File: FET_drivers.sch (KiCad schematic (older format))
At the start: 41 parts

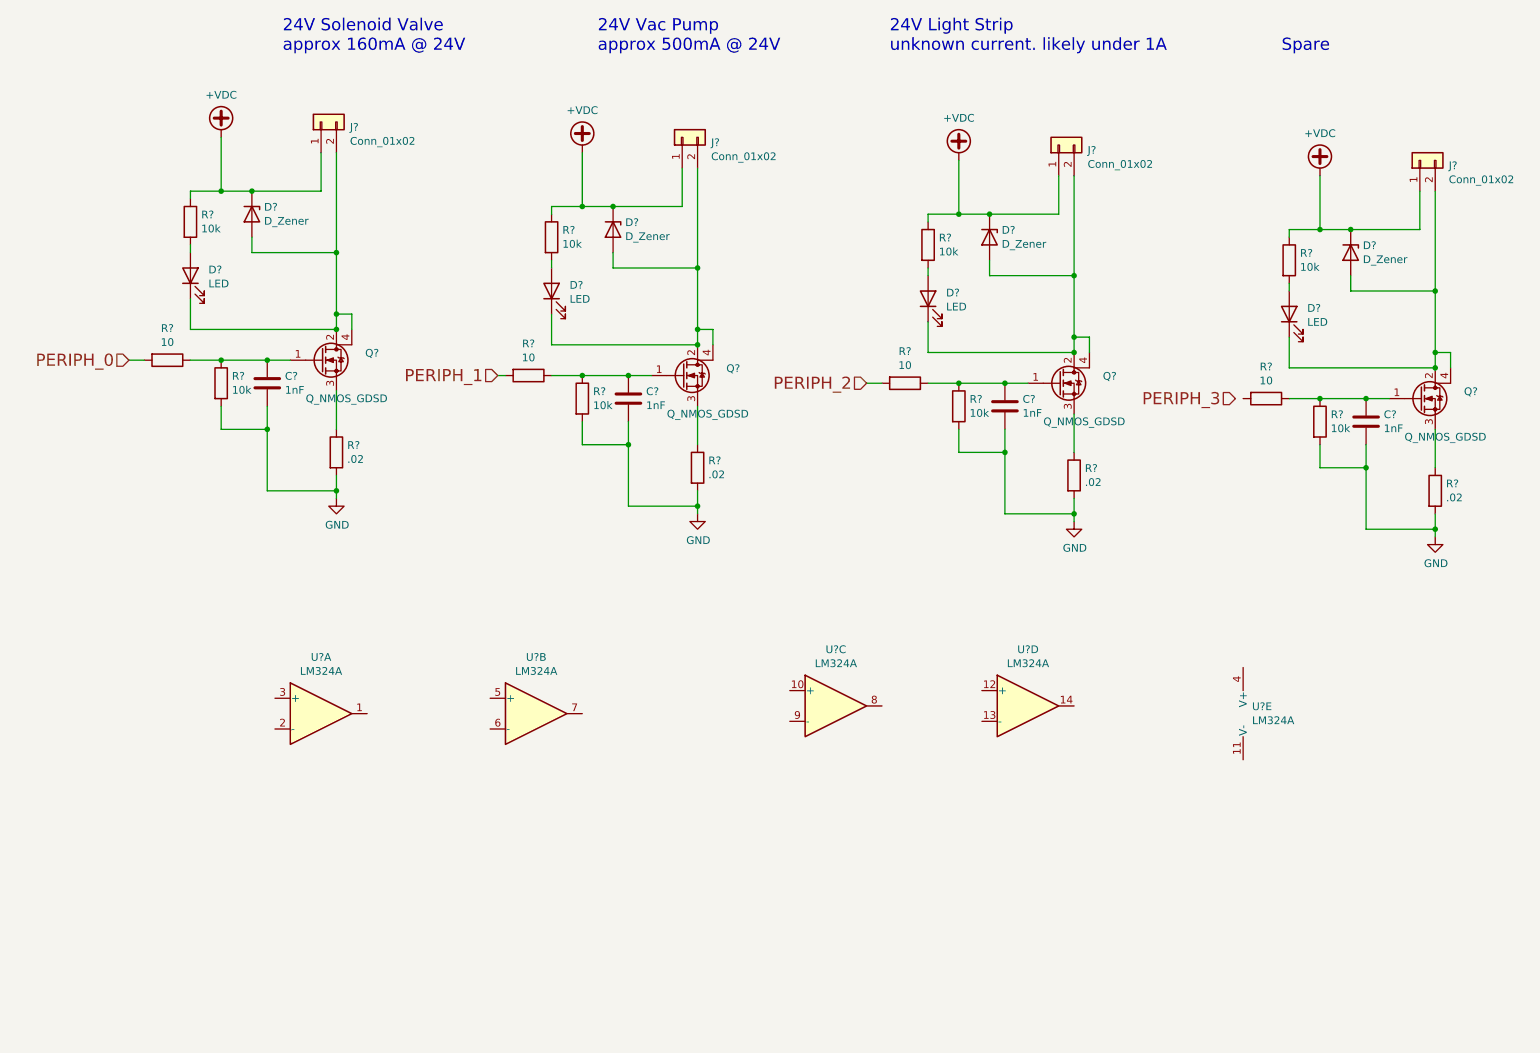
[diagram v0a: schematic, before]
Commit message: Added FET Drivers + PNs. Started Trinamic drivers
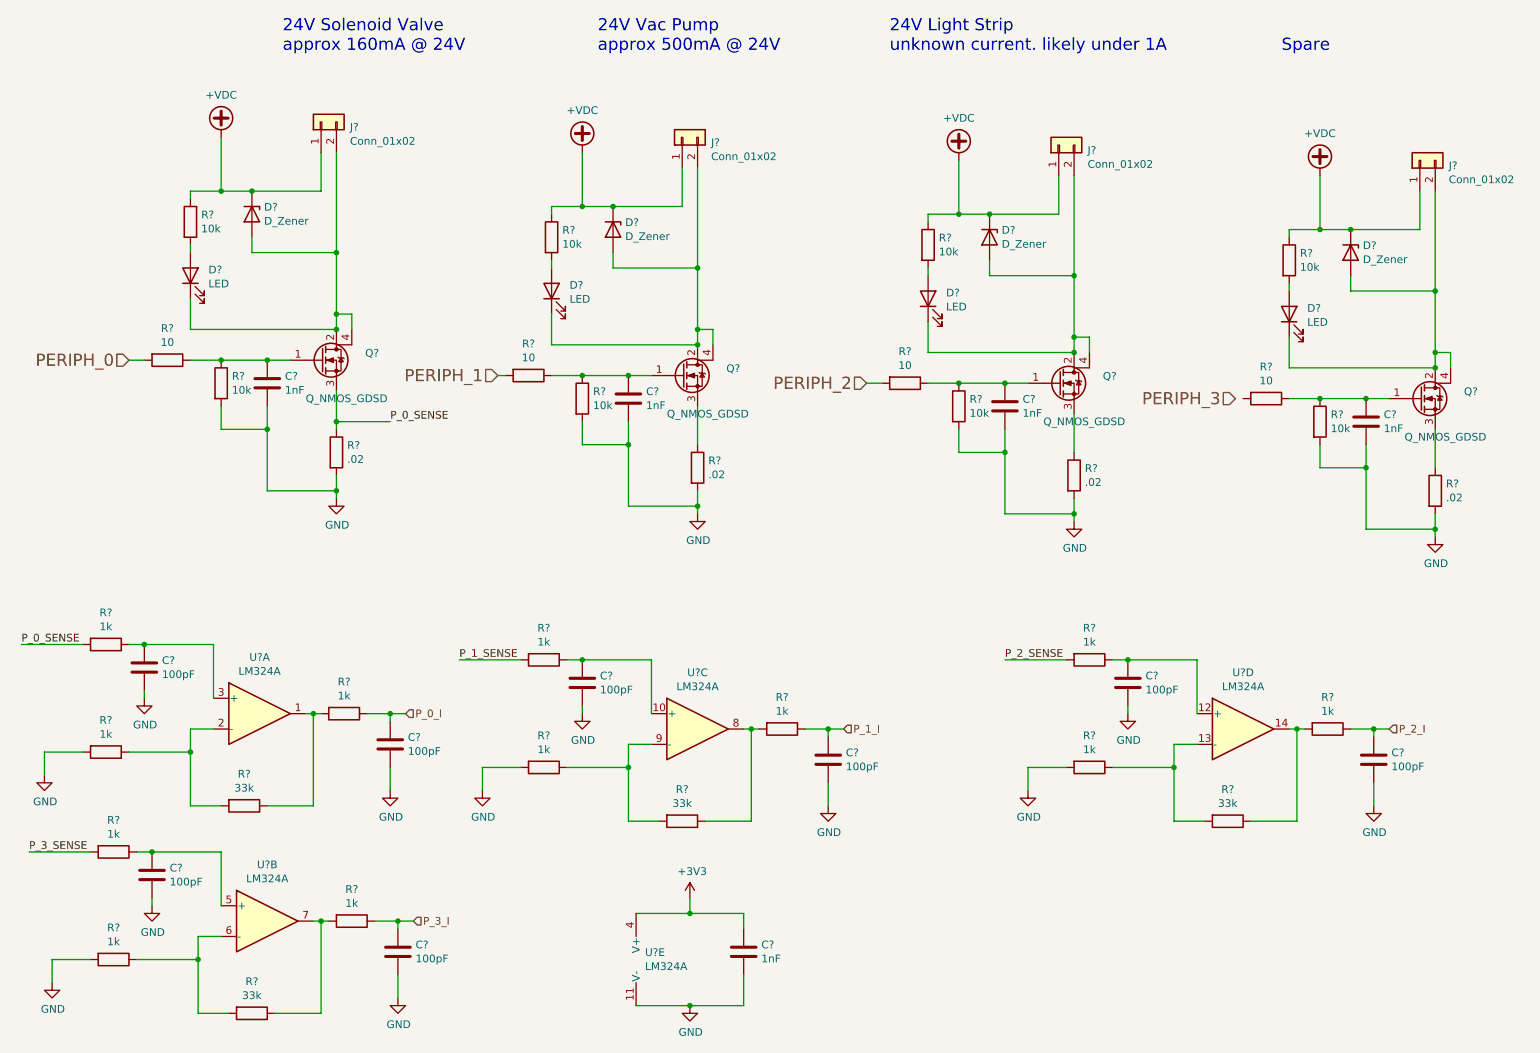
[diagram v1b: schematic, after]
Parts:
- added C? (x8): 100pF, Capacitors_SMD:C_0603_HandSoldering, symbol Device:C
- added C?: 1nF, Capacitors_SMD:C_0603_HandSoldering, symbol Device:C
- added R? (x12): 1k, Resistors_SMD:R_0603_HandSoldering, symbol Device:R
- added R? (x4): 33k, Resistors_SMD:R_0603_HandSoldering, symbol Device:R
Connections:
- net GND: now also U?.11 (V-), C?.2, C?.2, C?.2, C?.2, C?.2, C?.2, C?.2, C?.2, C?.2, R?.2, R?.2, R?.2, R?.2
- net P_0_SENSE: now reaches Q?.3 (S), R?.1
- net P_0_SENSE: now also R?.2
- net at U?.1: now also R?.1, R?.2
- net at U?.2 (-): now also R?.1, R?.2
- net at U?.3 (+): now also C?.1, R?.1
- net at U?.5 (+): now also C?.1, R?.1
- net at U?.6 (-): now also R?.1, R?.2
- net at U?.7: now also R?.1, R?.2
- net at U?.10 (+): now also C?.1, R?.1
- net at U?.8: now also R?.1, R?.2
- net at U?.9 (-): now also R?.1, R?.2
- net at U?.12 (+): now also C?.1, R?.1
- net at U?.13 (-): now also R?.1, R?.2
- net at U?.14: now also R?.1, R?.2
- net +3V3: now reaches U?.4 (V+)
- net +3V3: now also C?.1
- new net P_0_I: C?.1, R?.1
- new net P_1_I: C?.1, R?.1
- new net P_1_SENSE: R?.2
- new net P_2_I: C?.1, R?.1
- new net P_2_SENSE: R?.2
- new net P_3_I: C?.1, R?.1
- new net P_3_SENSE: R?.2
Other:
- moved on the sheet: U?A, U?B, U?C, U?D, U?E
